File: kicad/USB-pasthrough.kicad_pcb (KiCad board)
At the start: 4 copper layers, 40 x 80 mm, 93 parts, among them J1 USB_Power, J2 USB_C, J3 Cortex Debug, J4 Power_Sel, J5 SPI Display, J6 SWD, J7 USB_A, J8 MicroSD, SW1 Boot0, SW2 Reset, U1 AMS1117, U2 STM32F723VET6, Y1 8 MHz

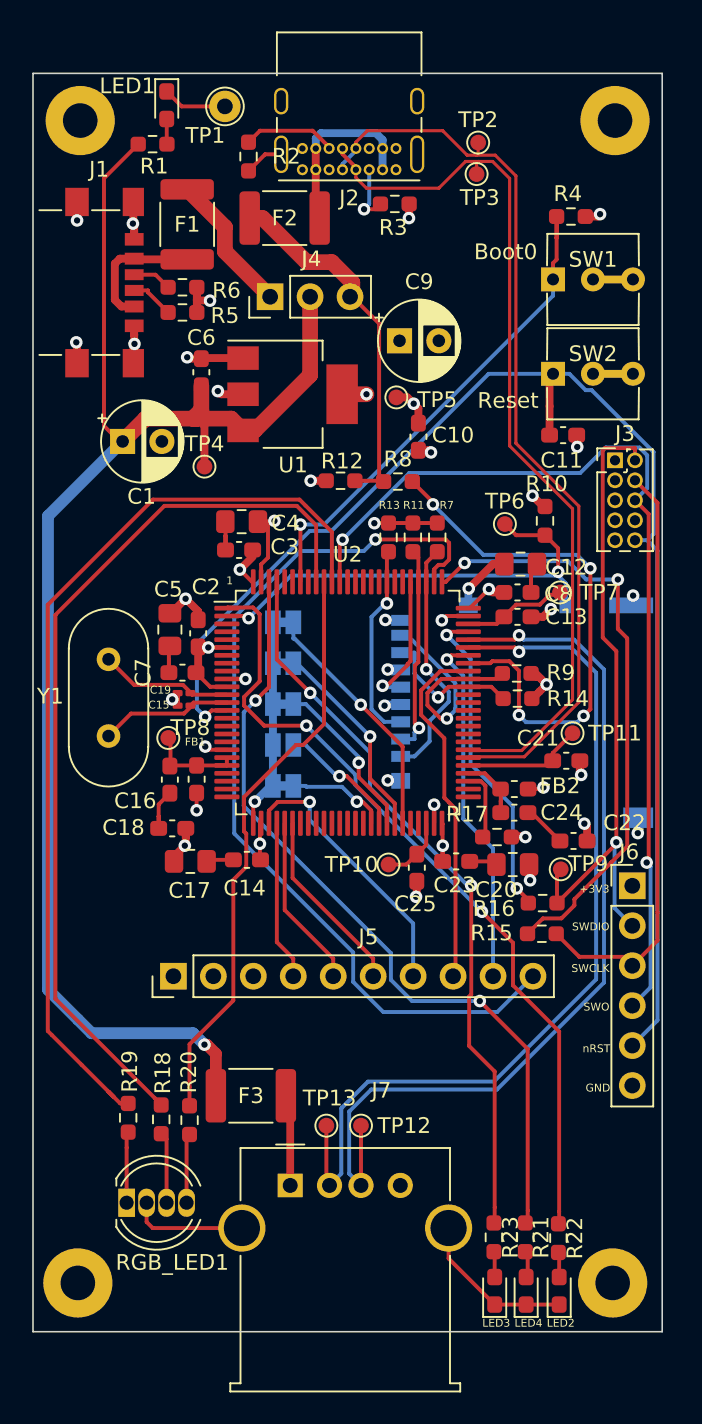
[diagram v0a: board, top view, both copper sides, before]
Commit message: Add fulsized SD Card connector serial etc...
Add KiCad symbol and footprint for SD Card connector to try out
overlaying Full size and uSD connectors allowing support for either
one depending on which connector is installed.

Also add SMD USB A connector for possible use in place of THT.
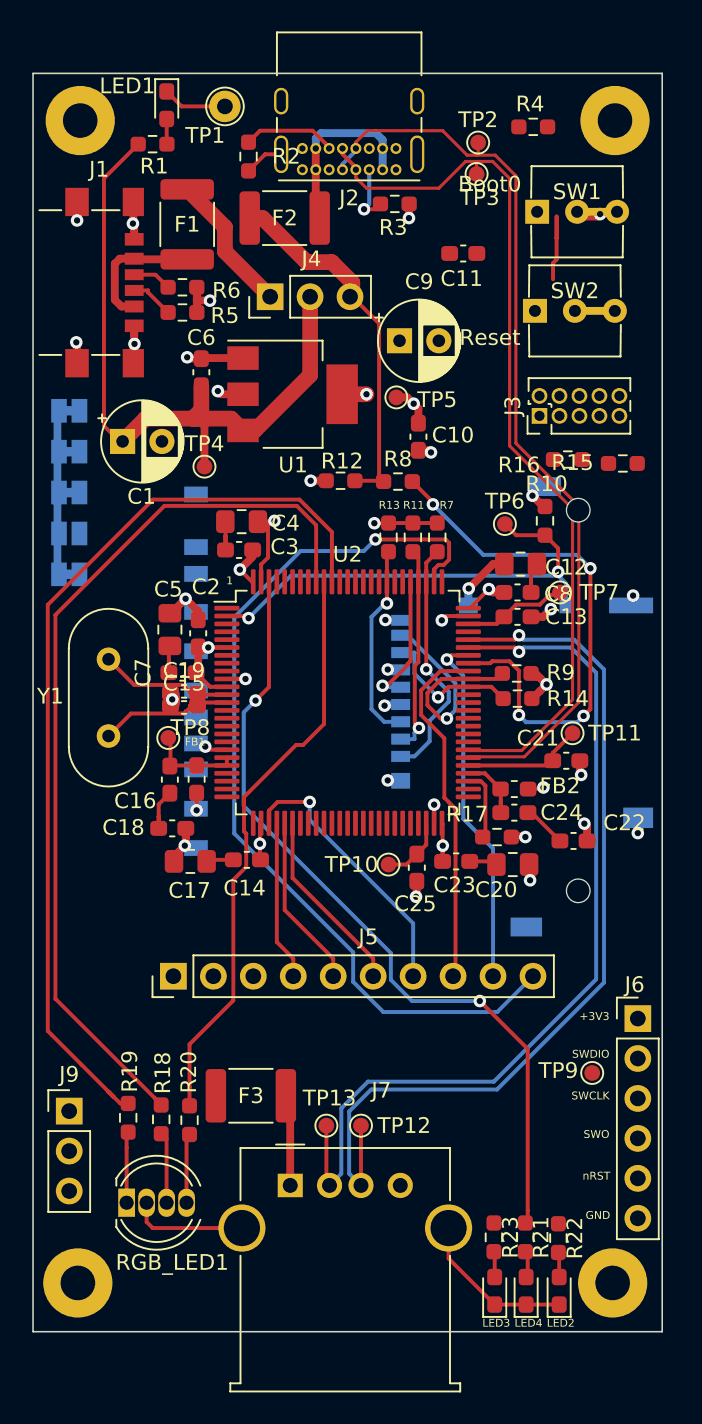
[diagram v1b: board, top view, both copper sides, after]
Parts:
- added J10: SD-1-A, SD-1-A:CUI_SD-1-A, B.Cu at (125.4, 89.9)
- added J9: Serial, Connector_PinHeader_2.54mm:PinHeader_1x03_P2.54mm_Vertical, F.Cu at (102.3, 116.0)
- C15, C19: footprint Capacitor_SMD:C_0201_0603Metric_Pad0.64x0.40mm_HandSolder -> Capacitor_SMD:C_0603_1608Metric_Pad1.08x0.95mm_HandSolder
- moved R15 30.3 mm to (137.5, 74.8)
- moved R16 28.2 mm to (134.0, 74.5)
- moved ID0 19.1 mm to (102.3, 81.8)
- moved ID1 19.1 mm to (102.3, 79.2)
- moved ID3 19.1 mm to (102.3, 74.0)
- moved ID4 19.1 mm to (102.3, 71.5)
- moved ID2 19.1 mm to (102.3, 76.7)
- moved C11 13.2 mm to (127.3, 61.5)
- moved TP9 13.1 mm to (135.6, 113.5)
- moved J6 8.45 mm to (138.4, 110.1)
- moved R4 6.18 mm to (131.8, 53.4)
- moved J3 5.57 mm to (132.2, 71.8), turned to 90 degrees
- moved SW1 4.42 mm to (132.1, 58.8)
- moved SW2 4.16 mm to (131.9, 65.1)
- renumbered ID5 to ID0, ID4 to ID1, ID3 to ID2, ID2 to ID3, ID1 to ID4
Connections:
- net /PA13 renamed /SWDIO_
- net /PA14 renamed /SWCLK_
- C16 pad 2: Net-(C16-Pad2) -> GND
- C18 pad 1: Net-(C16-Pad2) -> /VDDA
- C24 pad 1: Net-(C24-Pad1) -> Net-(C22-Pad1)
- C24 pad 2: Net-(C22-Pad1) -> GND
- FB2 pad 1: Net-(C24-Pad1) -> Net-(C22-Pad1)
- J6 pad 2: /SWDIO -> /SWCLK
- J6 pad 3: /SWCLK -> GND
- J6 pad 4: /SWO -> /SWDIO
- J6 pad 6: GND -> /SWO
- U2 pad 24: unconnected-(U2-Pad24) -> /TXD
- U2 pad 25: unconnected-(U2-Pad25) -> /RXD
- U2 pad 54: Net-(C24-Pad1) -> Net-(C22-Pad1)
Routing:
- net /nRESET: track 90.1 -> 18.4 mm
- net /SWO: track 61.1 -> 0.00 mm, vias 2 -> 0
- net +5V: track 97.4 -> 45.5 mm, vias 1 -> 0
- net /LED4: track 51.5 -> 0.00 mm, vias 2 -> 0
- net /LED2: track 46.8 -> 0.00 mm, vias 2 -> 0
- net /SWDIO: track 41.7 -> 0.00 mm, vias 1 -> 0
- net /SWCLK_: track 38.3 -> 0.00 mm, vias 2 -> 0
- net /SWCLK: track 38.1 -> 0.00 mm
- net Net-(R4-Pad1): track 32.2 -> 5.46 mm, vias 1 -> 0
- net /SWDIO_: track 20.5 -> 0.00 mm, vias 2 -> 0
- net Net-(ID4-Pad1): track 15.7 -> 0.00 mm, vias 1 -> 0
- net Net-(ID3-Pad1): track 13.0 -> 0.00 mm, vias 1 -> 0
- net Net-(ID2-Pad1): track 10.5 -> 0.00 mm, vias 1 -> 0
- net Net-(C19-Pad2): track 8.51 -> 0.00 mm
- net Net-(C15-Pad2): track 8.51 -> 0.00 mm
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
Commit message: First Pass v0.2 schematic
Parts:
- removed the C12 at (131.0, 81.2)
- removed the C17 at (110.0, 100.1)
- removed the C20 at (130.5, 100.3)
- removed the C4 at (113.3, 78.5)
- removed ID0: Jumper_2_Bridged, Jumper:SolderJumper-2_P1.3mm_Bridged_Pad1.0x1.5mm
- removed the TP11 at (134.3, 92.0)
- added C14: 4.7uF, Capacitor_SMD:C_0603_1608Metric_Pad1.08x0.95mm_HandSolder, F.Cu at (130.9, 81.6)
- added C15: 4.7uF, Capacitor_SMD:C_0603_1608Metric_Pad1.08x0.95mm_HandSolder, F.Cu at (110.0, 100.0)
- added C23: 4.7uF, Capacitor_SMD:C_0603_1608Metric_Pad1.08x0.95mm_HandSolder, F.Cu at (130.4, 100.0)
- added C5: 4.7uF, Capacitor_SMD:C_0603_1608Metric_Pad1.08x0.95mm_HandSolder, F.Cu at (113.0, 78.8)
- added ID5: Jumper_2_Bridged, Jumper:SolderJumper-2_P1.3mm_Open_Pad1.0x1.5mm, B.Cu at (120.0, 72.2)
- added R8: 10K, Resistor_SMD:R_0603_1608Metric_Pad0.98x0.95mm_HandSolder, F.Cu at (130.8, 87.7)
- added TP9: V12PHYHS, TestPoint:TestPoint_Pad_D1.0mm, F.Cu at (134.7, 92.0)
- C9: renamed from C5; footprint Capacitor_SMD:C_0805_2012Metric_Pad1.18x1.45mm_HandSolder -> Capacitor_SMD:C_0603_1608Metric_Pad1.08x0.95mm_HandSolder
- ID1: footprint Jumper:SolderJumper-2_P1.3mm_Open_Pad1.0x1.5mm -> Jumper:SolderJumper-2_P1.3mm_Bridged_Pad1.0x1.5mm
- TP12: value USBA+ -> USBA-
- TP13: value USBA- -> USBA+
- TP6: value MMC1_CDET -> SD1_CDET
- moved ID3 24.4 mm to (126.6, 72.2), turned to 90 degrees
- moved ID4 22.1 mm to (124.4, 72.2), turned to 90 degrees
- moved ID2 20.4 mm to (122.2, 72.2), turned to 90 degrees
- moved ID1 17.0 mm to (117.8, 72.2), turned to 90 degrees
- moved TP5 7.56 mm to (128.0, 64.8)
- moved C8 7.15 mm to (108.2, 78.8)
- moved TP8 5.96 mm to (107.5, 98.1)
- moved C6 4.35 mm to (107.8, 84.1)
- moved C9 2.76 mm to (107.8, 82.8), turned to 0 degrees
- moved U1 2.75 mm to (116.6, 67.7)
- moved C12 2.74 mm to (123.1, 70.8), turned to 0 degrees
- moved TP12 2.30 mm to (118.5, 117.0)
- moved J1 2.23 mm to (113.5, 62.6)
- moved TP13 2.20 mm to (120.8, 117.0)
- moved F2 2.17 mm to (118.1, 58.8), turned to 180 degrees
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- renumbered C11 to C1, C8 to C10, C13 to C11, C10 to C12, C9 to C13, C18 to C16, C14 to C17, C15 to C18, C16 to C19, C3 to C2, C22 to C20, C25 to C21, C23 to C22, C21 to C25, C1 to C3, C19 to C4, C7 to C6, C6 to C7, C2 to C8, J4 to J1, J8 to J10, J1 to J2, J2 to J3, J3 to J4, J9 to J7, J7 to J8, J10 to J9, LED3 to LED2, LED4 to LED3, LED2 to LED4, R2 to R1, R7 to R10, R10 to R12, R12 to R13, R13 to R14, R9 to R16, R14 to R18, R20 to R19, R1 to R2, R18 to R20, R19 to R21, R23 to R22, R21 to R23, R22 to R24, R6 to R5, R5 to R6, R16 to R7, R8 to R9, TP9 to TP11
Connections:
- net /MMC1_D1 renamed /SD1_D1
- net /MMC1_D3 renamed /SD1_D3
- C10 pad 2: Net-(C12-Pad2) -> GND
- C17 pad 1: Net-(C14-Pad1) -> GND
- C2 pad 1: Net-(C3-Pad1) -> GND
- C22 pad 2: Net-(C20-Pad1) -> GND
- C6 pad 1: Net-(C5-Pad2) -> GND
- C9 pad 2: Net-(C5-Pad2) -> +3V3
- ID1 pad 1: Net-(ID1-Pad1) -> Net-(U2-Pad58)
- ID2 pad 1: Net-(ID2-Pad1) -> Net-(U2-Pad60)
- ID3 pad 1: Net-(ID3-Pad1) -> Net-(U2-Pad62)
- ID4 pad 1: Net-(ID4-Pad1) -> Net-(U2-Pad61)
- J10 pad 1: /MMC1_D2 -> /SD1_D2
- J10 pad 10: /MMC1_CDET -> /SD1_CDET
- J10 pad 3: /MMC1_CMD -> /SD1_CMD
- J10 pad 5: /MMC1_CLK -> /SD1_CLK
- J10 pad 7: /MMC1_D0 -> /SD1_D0
- J9 pad 1: unconnected-(J10-Pad1) -> /SD1_D2
- J9 pad 2: unconnected-(J10-Pad2) -> /SD1_CMD
- J9 pad 3: unconnected-(J10-Pad3) -> GND
- J9 pad 4: unconnected-(J10-Pad4) -> +3V3
- J9 pad 5: unconnected-(J10-Pad5) -> /SD1_CLK
- J9 pad 6: unconnected-(J10-Pad6) -> GND
- J9 pad 7: unconnected-(J10-Pad7) -> /SD1_D0
- J9 pad 8: unconnected-(J10-Pad8) -> /SD1_D0
- J9 pad 9: unconnected-(J10-Pad9) -> /SD1_D2
- J9 pad CD: unconnected-(J10-PadCD) -> /SD1_CDET
- J9 pad G1: unconnected-(J10-PadG1) -> GND
- J9 pad G2: unconnected-(J10-PadG2) -> GND
- R10 pad 2: /MMC1_D2 -> /SD1_D2
- R12 pad 2: /MMC1_CDET -> /SD1_CDET
- R14 pad 2: /MMC1_CMD -> /SD1_CMD
- R18 pad 1: /MMC1_D0 -> /SD1_D0
- TP12 pad 1: /USBA+ -> /USBA-
- TP13 pad 1: /USBA- -> /USBA+
- TP6 pad 1: /MMC1_CDET -> /SD1_CDET
- U2 pad 1: /LED4 -> unconnected-(U2-Pad1)
- U2 pad 2: /MMC1_CDET -> /SD1_CDET
- U2 pad 23: unconnected-(U2-Pad23) -> /LCD_RST
- U2 pad 39: unconnected-(U2-Pad39) -> /LED2
- U2 pad 41: Net-(ID0-Pad1) -> /LED3
- U2 pad 42: Net-(ID1-Pad1) -> unconnected-(U2-Pad42)
- U2 pad 43: Net-(ID2-Pad1) -> /LED4
- U2 pad 44: Net-(ID3-Pad1) -> unconnected-(U2-Pad44)
- U2 pad 45: Net-(ID4-Pad1) -> unconnected-(U2-Pad45)
- U2 pad 58: unconnected-(U2-Pad58) -> Net-(U2-Pad58)
- U2 pad 59: unconnected-(U2-Pad59) -> Net-(U2-Pad59)
- U2 pad 60: unconnected-(U2-Pad60) -> Net-(U2-Pad60)
- U2 pad 61: unconnected-(U2-Pad61) -> Net-(U2-Pad61)
- U2 pad 62: unconnected-(U2-Pad62) -> Net-(U2-Pad62)
- U2 pad 65: /MMC1_D0 -> /SD1_D0
- U2 pad 69: /LCD_RST -> /OTG_FS_ID
- U2 pad 78: /MMC1_D2 -> /SD1_D2
- U2 pad 80: /MMC1_CLK -> /SD1_CLK
- U2 pad 83: /MMC1_CMD -> /SD1_CMD
- U2 pad 97: /LED2 -> unconnected-(U2-Pad97)
- U2 pad 98: /LED3 -> unconnected-(U2-Pad98)
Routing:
- net Net-(U2-Pad60): track 0.00 -> 126.6 mm, vias 0 -> 3
- net /nRESET: track 18.4 -> 111.3 mm, vias 1 -> 2
- net /SWO: track 0.00 -> 89.4 mm, vias 0 -> 2
- net Net-(U2-Pad61): track 0.00 -> 89.3 mm, vias 0 -> 5
- net /USBC+: track 57.0 -> 124.7 mm, vias 0 -> 1
- net /SD1_CMD: track 0.00 -> 65.8 mm, vias 0 -> 3
- net /USBC-: track 58.2 -> 1.70 mm
- net /SWDIO: track 0.00 -> 52.2 mm
- net /SWCLK: track 0.00 -> 51.0 mm
- net Net-(U2-Pad58): track 0.00 -> 50.9 mm, vias 0 -> 1
- net +5V: track 45.5 -> 96.2 mm
- net /SD1_CDET: track 0.00 -> 42.8 mm, vias 0 -> 5
- net Net-(U2-Pad59): track 0.00 -> 41.0 mm, vias 0 -> 3
- net Net-(R4-Pad1): track 5.46 -> 42.0 mm, vias 0 -> 1
- net /LED4: track 0.00 -> 35.1 mm
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
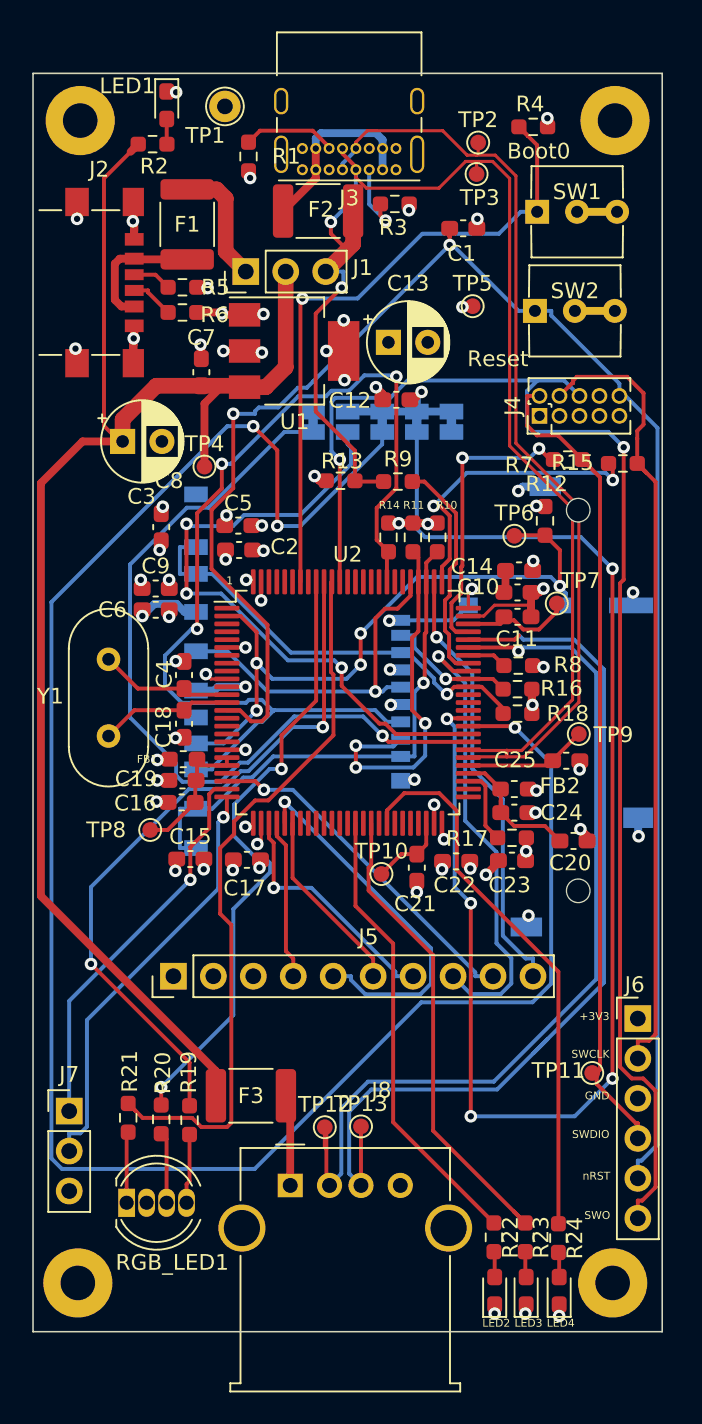
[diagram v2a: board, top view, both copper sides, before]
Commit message: Test routing, many courtyard conflicts
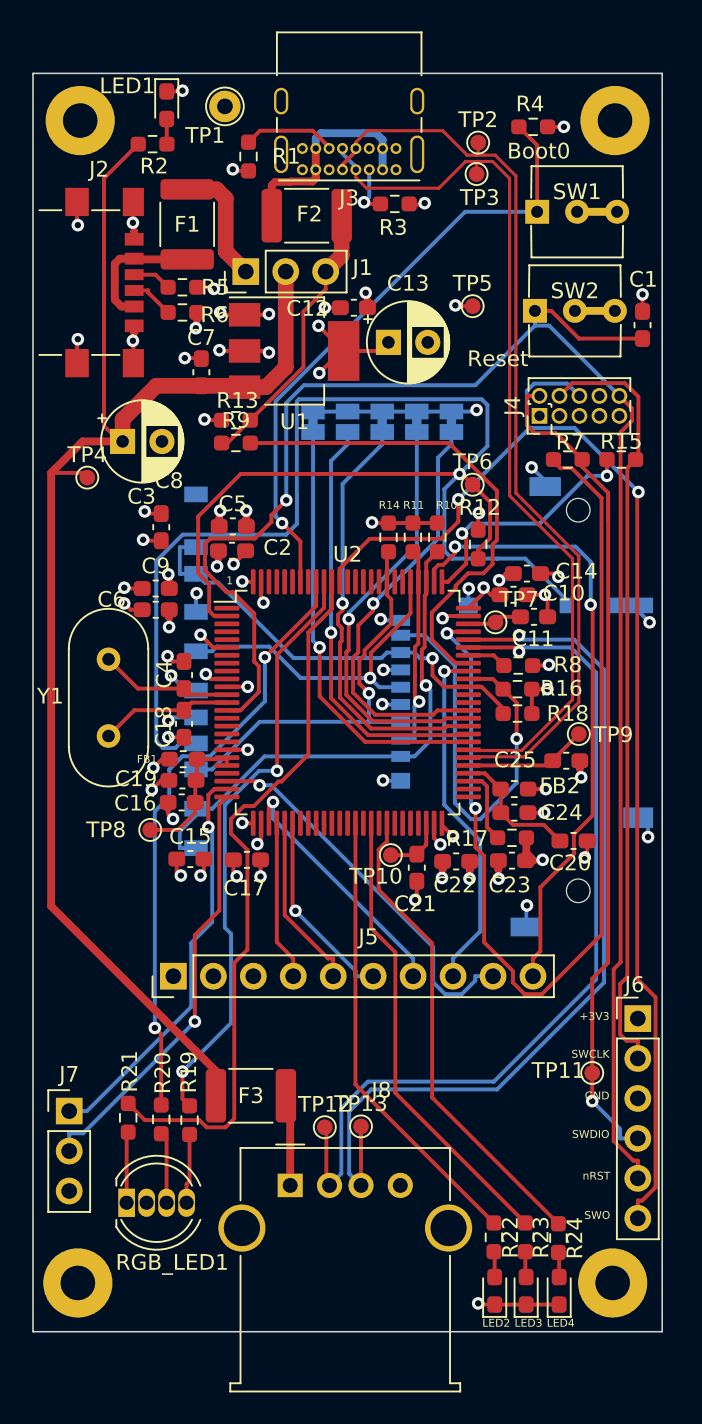
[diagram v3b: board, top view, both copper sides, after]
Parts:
- moved C1 13.0 mm to (138.8, 66.0), turned to 90 degrees
- moved R9 10.6 mm to (112.9, 73.5)
- moved R13 7.68 mm to (112.9, 72.0)
- moved TP4 7.48 mm to (103.5, 75.7)
- moved C12 6.44 mm to (120.4, 64.9)
- moved R12 4.51 mm to (128.3, 80.0)
- moved TP6 4.19 mm to (128.0, 76.2)
- moved TP7 4.08 mm to (129.4, 84.9)
- moved TP10 1.34 mm to (122.8, 99.7)
- moved C11 1.05 mm to (131.8, 84.5)
- moved F2 0.78 mm to (117.4, 59.0)
- moved C14 0.54 mm to (131.4, 81.8)
- moved C2 0.45 mm to (112.7, 80.3)
- moved C5 0.35 mm to (112.7, 78.8)
- moved C10 0.29 mm to (130.6, 83.2)
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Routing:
- net Net-(U2-Pad60): track 126.6 -> 27.2 mm, vias 3 -> 1
- net /USBC+: track 124.7 -> 57.0 mm, vias 1 -> 0
- net Net-(U2-Pad61): track 89.3 -> 27.1 mm, vias 5 -> 1
- net /USBC-: track 1.70 -> 58.2 mm
- net /SD1_CDET: track 42.8 -> 96.0 mm, vias 5 -> 1
- net /SWDIO_: track 18.6 -> 64.7 mm
- net /SD1_CMD: track 65.8 -> 26.3 mm, vias 3 -> 1
- net Net-(U2-Pad62): track 0.00 -> 27.2 mm, vias 0 -> 1
- net Net-(U2-Pad58): track 50.9 -> 27.6 mm
- net /SD1_D1: track 8.39 -> 27.1 mm
- net Net-(R8-Pad2): track 14.5 -> 31.6 mm
- net GND: track 71.9 -> 89.0 mm, vias 50 -> 54
- net +3V3: track 34.7 -> 48.7 mm
- net Net-(U2-Pad59): track 41.0 -> 27.1 mm, vias 3 -> 1
- net /SPI1_MISO: track 23.9 -> 11.2 mm, vias 1 -> 0
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
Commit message: V0.2 layout pending bring-up
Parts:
- removed the C7 at (110.7, 69.0)
- added C2: 100nF, Capacitor_SMD:C_0603_1608Metric_Pad1.08x0.95mm_HandSolder, F.Cu at (109.2, 68.4)
- moved R4 19.3 mm to (128.2, 60.2), turned to 180 degrees
- moved R3 19.3 mm to (128.2, 61.7)
- moved ID1 9.85 mm to (127.7, 72.2)
- moved ID5 9.15 mm to (117.5, 72.2)
- moved R6 8.23 mm to (127.7, 51.5)
- moved TP3 5.34 mm to (123.2, 62.5)
- moved ID2 5.10 mm to (125.1, 72.2)
- moved ID4 4.40 mm to (120.0, 72.2)
- moved U1 3.98 mm to (114.0, 70.7), turned to -90 degrees
- moved C13 3.25 mm to (119.8, 68.1)
- moved TP5 2.80 mm to (103.5, 78.5)
- moved C10 2.07 mm to (124.0, 65.6)
- moved C5 2.05 mm to (107.7, 72.8), turned to 180 degrees
- moved J3 1.92 mm to (114.7, 64.1)
- moved R1 1.80 mm to (109.4, 54.5), turned to 180 degrees
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- renumbered C6 to C1, C13 to C10, C14 to C11, C1 to C12, C12 to C13, C11 to C14, C17 to C15, C15 to C16, C16 to C17, C19 to C18, C18 to C19, C22 to C20, C20 to C21, C25 to C22, C24 to C23, C21 to C24, C23 to C25, C2 to C3, C5 to C4, C3 to C5, C4 to C6, C8 to C7, C9 to C8, C10 to C9, ID5 to ID2, ID2 to ID3, ID3 to ID5, J2 to J1, J3 to J2, J1 to J3, R2 to R1, R15 to R10, R12 to R11, R8 to R12, R14 to R13, R10 to R14, R7 to R15, R18 to R16, R16 to R17, R17 to R18, R21 to R19, R1 to R2, R19 to R20, R20 to R21, R23 to R22, R22 to R23, R9 to R3, R13 to R4, R4 to R5, R3 to R6, R5 to R7, R6 to R8, R11 to R9, TP5 to TP3, TP3 to TP4, TP4 to TP5, TP7 to TP6, TP6 to TP7
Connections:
- ID1 pad 1: Net-(U2-Pad58) -> Net-(ID1-Pad1)
- ID2 pad 1: Net-(U2-Pad59) -> Net-(ID2-Pad1)
- ID3 pad 1: Net-(U2-Pad60) -> Net-(ID3-Pad1)
- ID4 pad 1: Net-(U2-Pad61) -> Net-(ID4-Pad1)
- ID5 pad 1: Net-(U2-Pad62) -> Net-(ID5-Pad1)
- J9 pad 1: /SD1_D2 -> /SD1_D3
- J9 pad 8: /SD1_D0 -> /SD1_D1
- U2 pad 58: Net-(U2-Pad58) -> unconnected-(U2-Pad58)
- U2 pad 59: Net-(U2-Pad59) -> unconnected-(U2-Pad59)
- U2 pad 60: Net-(U2-Pad60) -> unconnected-(U2-Pad60)
- U2 pad 61: Net-(U2-Pad61) -> unconnected-(U2-Pad61)
- U2 pad 62: Net-(U2-Pad62) -> unconnected-(U2-Pad62)
- U2 pad 84: unconnected-(U2-Pad84) -> Net-(ID1-Pad1)
- U2 pad 85: unconnected-(U2-Pad85) -> Net-(ID2-Pad1)
- U2 pad 86: unconnected-(U2-Pad86) -> Net-(ID3-Pad1)
- U2 pad 87: unconnected-(U2-Pad87) -> Net-(ID4-Pad1)
- U2 pad 88: unconnected-(U2-Pad88) -> Net-(ID5-Pad1)
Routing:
- net /SD1_CDET: track 96.0 -> 60.3 mm, vias 1 -> 2
- net Net-(U2-Pad58): track 27.6 -> 0.00 mm, vias 1 -> 0
- net Net-(U2-Pad60): track 27.2 -> 0.00 mm, vias 1 -> 0
- net Net-(U2-Pad62): track 27.2 -> 0.00 mm, vias 1 -> 0
- net Net-(U2-Pad61): track 27.1 -> 0.00 mm, vias 1 -> 0
- net Net-(U2-Pad59): track 27.1 -> 0.00 mm, vias 1 -> 0
- net /SD1_D1: track 27.1 -> 46.1 mm
- net Net-(ID1-Pad1): track 0.00 -> 18.6 mm, vias 0 -> 1
- net Net-(ID4-Pad1): track 0.00 -> 17.8 mm, vias 0 -> 1
- net Net-(ID2-Pad1): track 0.00 -> 17.2 mm, vias 0 -> 1
- net Net-(ID5-Pad1): track 0.00 -> 15.9 mm, vias 0 -> 1
- net /SD1_D3: track 13.3 -> 28.1 mm
- net +5V: track 91.4 -> 81.2 mm
- net Net-(ID3-Pad1): track 0.00 -> 10.2 mm, vias 0 -> 1
- net GND: track 89.0 -> 96.9 mm, vias 54 -> 53
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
